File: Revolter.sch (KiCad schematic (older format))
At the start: 31 parts, among them J1 IO, J2 USB_A, P2 CAN, P3 IN+, P4 IN-, P5 MOTOR3, P6 MOTOR2, P7 MOTOR1, P9 Motor

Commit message: - removed lots of unused circuitry - implemented new DMOS power stage - power supplies still missing - removed rescue lib and fixed referenced
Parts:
- removed J1: IO, Connector_Phoenix_MC:PhoenixContact_MCV_1,5_8-G-3.5_1x08_P3.50mm_Vertical, symbol Revolter-rescue:Conn_01x08-conn
- removed JP1: Jumper_NC_Dual, Jumper:SolderJumper-3_P1.3mm_Open_RoundedPad1.0x1.5mm, symbol Device:Jumper_NC_Dual
- removed JP3, JP4: opt., Jumper:SolderJumper-2_P1.3mm_Open_RoundedPad1.0x1.5mm, symbol Device:Jumper_NC_Small
- removed P2: CAN, Connector_Phoenix_MC:PhoenixContact_MCV_1,5_4-G-3.5_1x04_P3.50mm_Vertical, symbol Revolter-rescue:CONN_01X04
- removed P9: Motor, Connector_Phoenix_MC:PhoenixContact_MCV_1,5_6-G-3.5_1x06_P3.50mm_Vertical, symbol Revolter-rescue:CONN_01X06
- removed R11, R61: 1k, Resistor_SMD:R_0805_2012Metric, symbol Device:R
- removed R62, R63: 1k5, Resistor_SMD:R_0805_2012Metric, symbol Device:R
- D13: symbol Revolter-rescue:ZENER-RESCUE-Revolter -> Device:D_Zener
- D2: value LED -> BLUE; symbol Revolter-rescue:LED-RESCUE-BLDC_4 -> Device:LED
- D3, D4: symbol Revolter-rescue:LED-RESCUE-BLDC_4 -> Device:LED
- J2: symbol Revolter-rescue:USB_A-conn -> Connector:USB_A
- P3, P4, P5, P6, P7: symbol Revolter-rescue:CONN_1 -> Connector_Generic:Conn_01x01
- R10, R4, R5, R6: symbol Revolter-rescue:R-RESCUE-BLDC_4 -> Device:R
- R9: symbol Revolter-rescue:R-RESCUE-BLDC_4 -> Device:Thermistor_NTC
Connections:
- net labels removed: +12V, +5V
- wire segments 90 -> 30
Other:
- note added: "REVOLTER 40V"
- note removed: "REVOLTER 100V"
- moved on the sheet: R8

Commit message: - added temp sensors and fan/pump outputs - made footprint selection
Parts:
- removed J2: USB_A, Connector_USB:USB_B_TE_5787834_Vertical, symbol Connector:USB_A
- added J1: Motor, symbol Connector_Generic:Conn_01x06
- added J2: TEMP, symbol Connector_Generic:Conn_01x12
- added J3: USB_B_Mini, Connector_USB:USB_Mini-B_Tensility_54-00023_Vertical, symbol Connector:USB_B_Mini
- added Q1, Q2, Q3: Q_NMOS_GSD, Package_TO_SOT_SMD:SOT-23, symbol Device:Q_NMOS_GSD
- added RN1, RN2, RN3: 10k, Resistor_SMD:R_Array_Convex_4x0603, symbol Device:R_Pack04
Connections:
- net labels added: +12V, FAN1, FAN2, PUMP, TEMP1, TEMP2, TEMP3
- wire segments 30 -> 79
- no-connect marks 0 -> 6
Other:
- moved on the sheet: P5, P6, P7

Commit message: - did most of the layout
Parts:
- removed D13: 3V3, Diode_SMD:D_SOD-123, symbol Device:D_Zener
- J1: footprint (none) -> Connector_PinHeader_2.00mm:PinHeader_1x06_P2.00mm_Vertical
- J2: footprint (none) -> Connector_PinHeader_2.00mm:PinHeader_1x12_P2.00mm_Vertical
- R4: value 470R -> 120R
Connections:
- wire segments 79 -> 78
- no-connect marks 6 -> 4
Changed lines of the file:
@@
 P 4750 5350
 F 0 "R4" V 4650 5350 50  0000 C CNN
-F 1 "470R" V 4750 5350 50  0000 C CNN
+F 1 "120R" V 4750 5350 50  0000 C CNN
 F 2 "Resistor_SMD:R_0805_2012Metric" H 4750 5350 60  0001 C CNN
 F 3 "" H 4750 5350 60  0001 C CNN
@@
 Wire Wire Line
 	5950 3700 5950 6500
-$Comp
-L Device:D_Zener D13
-U 1 1 599A9D56
-P 5450 4650
-F 0 "D13" H 5450 4750 50  0000 C CNN
-F 1 "3V3" H 5450 4550 50  0000 C CNN
-F 2 "Diode_SMD:D_SOD-123" H 5450 4650 50  0001 C CNN
-F 3 "" H 5450 4650 50  0000 C CNN
-	1    5450 4650
-	0    1    1    0
-$EndComp
-$Comp
-L power:GND #PWR015
-U 1 1 599AD91E
-P 5450 4800
-F 0 "#PWR015" H 5450 4800 30  0001 C CNN
-F 1 "GND" H 5450 4730 30  0001 C CNN
-F 2 "" H 5450 4800 60  0001 C CNN
-F 3 "" H 5450 4800 60  0001 C CNN
-	1    5450 4800
-	1    0    0    -1
-$EndComp
-Wire Wire Line
-	5200 4500 5450 4500
 Wire Wire Line
 	4300 3600 6150 3600
@@
 	2650 7050 2650 6600
 Wire Wire Line
-	2550 5100 2550 6250
-Wire Wire Line
-	2550 5100 2950 5100
+	2450 5100 2450 6250
+Wire Wire Line
+	2450 5100 2950 5100
 $Comp
 L power:GND #PWR0182
@@
 F 0 "J2" H 650 4600 50  0000 C CNN
 F 1 "TEMP" V 750 5300 50  0000 C CNN
-F 2 "" H 650 5300 50  0001 C CNN
+F 2 "Connector_PinHeader_2.00mm:PinHeader_1x12_P2.00mm_Vertical" H 650 5300 50  0001 C CNN
 F 3 "~" H 650 5300 50  0001 C CNN
 	1    650  5300
@@
 Connection ~ 2650 4900
 Wire Wire Line
-	1500 6250 2550 6250
+	1500 6250 2450 6250
 Wire Wire Line
 	1900 6600 2650 6600
@@
 Wire Wire Line
 	2000 7350 2000 7150
-$Comp
-L power:+3V3 #PWR0191
-U 1 1 5EF7F583
-P 2450 3650
-F 0 "#PWR0191" H 2450 3500 50  0001 C CNN
-F 1 "+3V3" H 2450 3850 50  0000 C CNN
-F 2 "" H 2450 3650 60  0000 C CNN
-F 3 "" H 2450 3650 60  0000 C CNN
-	1    2450 3650
-	-1   0    0    -1
-$EndComp
-Wire Wire Line
-	2450 4200 2450 4050
-Wire Wire Line
-	2150 4300 2150 4050
+Wire Wire Line
+	2050 4300 2050 4050
 $Comp
 L power:GND #PWR0192
@@
 F 0 "J1" H 650 4600 50  0000 C CNN
 F 1 "Motor" V 750 4300 50  0000 C CNN
-F 2 "" H 650 4300 50  0001 C CNN
+F 2 "Connector_PinHeader_2.00mm:PinHeader_1x06_P2.00mm_Vertical" H 650 4300 50  0001 C CNN
 F 3 "~" H 650 4300 50  0001 C CNN
 	1    650  4300
@@
 $EndComp
 Wire Wire Line
-	2950 4200 2450 4200
-Connection ~ 2450 4200
-Wire Wire Line
-	2450 4200 850  4200
-Wire Wire Line
-	850  4300 2150 4300
-Connection ~ 2150 4300
-Wire Wire Line
-	2150 4300 2950 4300
+	850  4300 2050 4300
+Connection ~ 2050 4300
+Wire Wire Line
+	2050 4300 2950 4300
 $Comp
 L Device:R_Pack04 RN2
@@
 	1    0    0    -1
 $EndComp
-Wire Wire Line
-	1600 5000 2550 5000
-Wire Wire Line
-	2550 4050 2550 5000
-Connection ~ 2550 5000
-Wire Wire Line
-	2550 5000 2950 5000
 $Comp
 L power:+3V3 #PWR0194
@@
 $EndComp
 Wire Wire Line
-	850  4400 2050 4400
-Wire Wire Line
-	850  4500 1950 4500
-Wire Wire Line
-	2050 4050 2050 4400
-Connection ~ 2050 4400
-Wire Wire Line
-	2050 4400 2950 4400
-Wire Wire Line
-	1950 4050 1950 4500
-Connection ~ 1950 4500
-Wire Wire Line
-	1950 4500 2950 4500
+	850  4400 1950 4400
+Wire Wire Line
+	850  4500 1850 4500
+Wire Wire Line
+	1950 4050 1950 4400
+Connection ~ 1950 4400
+Wire Wire Line
+	1950 4400 2950 4400
+Wire Wire Line
+	1850 4050 1850 4500
+Connection ~ 1850 4500
+Wire Wire Line
+	1850 4500 2950 4500
 $Comp
 L Device:R_Pack04 RN3
@@
 	1    0    0    -1
 $EndComp
-Wire Wire Line
-	2550 6250 2550 7050
-Connection ~ 2550 6250
 $Comp
 L power:GND #PWR0197
@@
 	1    0    0    -1
 $EndComp
-NoConn ~ 1850 3650
-NoConn ~ 1850 4050
-NoConn ~ 2450 7050
-NoConn ~ 2450 7450
 $Comp
 L Connector_Generic:Conn_01x01 P7
@@
 Wire Wire Line
 	8150 2850 7650 2850
+$Comp
+L power:+3V3 #PWR0164
+U 1 1 5F0837B1
+P 1850 3650
+F 0 "#PWR0164" H 1850 3500 50  0001 C CNN
+F 1 "+3V3" H 1850 3850 50  0000 C CNN
+F 2 "" H 1850 3650 60  0000 C CNN
+F 3 "" H 1850 3650 60  0000 C CNN
+	1    1850 3650
+	-1   0    0    -1
+$EndComp
+Wire Wire Line
+	2150 4050 2150 4200
+Connection ~ 2150 4200
+Wire Wire Line
+	2150 4200 850  4200
+Wire Wire Line
+	2150 4200 2950 4200
+Wire Wire Line
+	1600 5000 2450 5000
+NoConn ~ 2550 4050
+Wire Wire Line
+	2450 4050 2450 5000
+Connection ~ 2450 5000
+Wire Wire Line
+	2450 5000 2950 5000
+$Comp
+L power:+3V3 #PWR0165
+U 1 1 5F09E502
+P 2450 3650
+F 0 "#PWR0165" H 2450 3500 50  0001 C CNN
+F 1 "+3V3" H 2450 3850 50  0000 C CNN
+F 2 "" H 2450 3650 60  0000 C CNN
+F 3 "" H 2450 3650 60  0000 C CNN
+	1    2450 3650
+	-1   0    0    -1
+$EndComp
+Wire Wire Line
+	2450 7050 2450 6250
+Connection ~ 2450 6250
+$Comp
+L power:GND #PWR0175
+U 1 1 5F0ABB53
+P 2450 7450
+F 0 "#PWR0175" H 2450 7200 50  0001 C CNN
+F 1 "GND" H 2450 7200 50  0000 C CNN
+F 2 "" H 2450 7450 50  0001 C CNN
+F 3 "" H 2450 7450 50  0001 C CNN
+	1    2450 7450
+	1    0    0    -1
+$EndComp
+NoConn ~ 2550 7050
 $EndSCHEMATC

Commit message: - changed current sensors - updated symbols - exported for production
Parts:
- NT1: symbol Device:Net-Tie_2 -> Device:NetTie_2
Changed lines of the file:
@@
 	4300 3600 6150 3600
 $Comp
-L Device:Net-Tie_2 NT1
+L Device:NetTie_2 NT1
 U 1 1 5C9626AB
 P 8650 4800

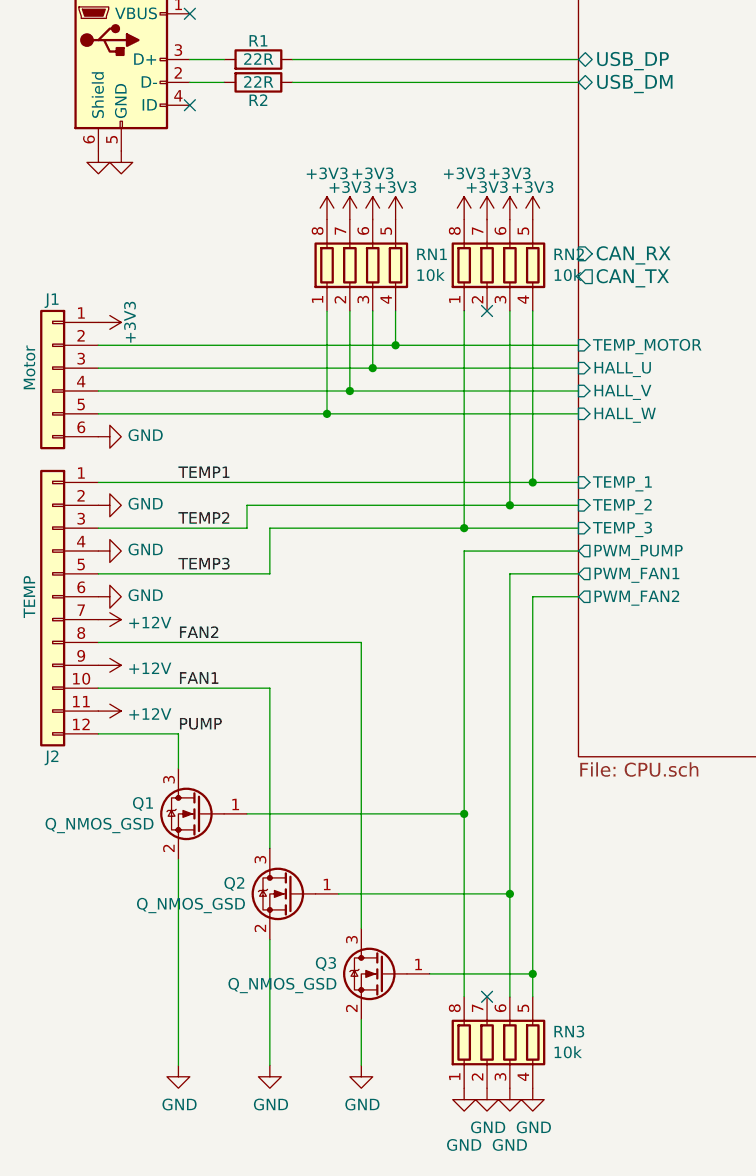
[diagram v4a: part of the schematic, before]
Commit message: - shrink PCB to 50x50mm
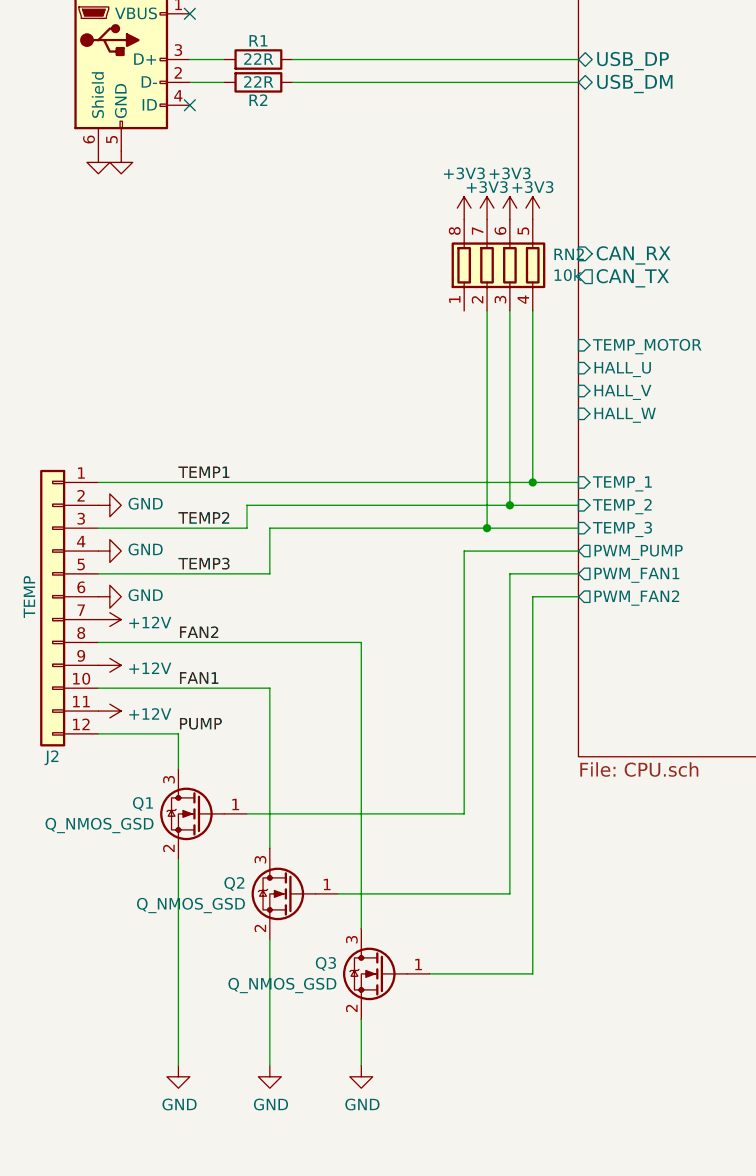
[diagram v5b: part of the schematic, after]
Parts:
- removed J1: Motor, Connector_PinHeader_2.00mm:PinHeader_1x06_P2.00mm_Vertical, symbol Connector_Generic:Conn_01x06
- removed RN1, RN3: 10k, Resistor_SMD:R_Array_Convex_4x0603, symbol Device:R_Pack04
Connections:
- net TEMP3: now also RN2.2 (R2.1); no longer RN2.1 (R1.1)
- no-connect marks 4 -> 2
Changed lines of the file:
@@
 	2950 5200 2650 5200
 Wire Wire Line
-	2750 7050 2750 6950
-Wire Wire Line
 	2750 5300 2950 5300
-Wire Wire Line
-	2650 7050 2650 6600
 Wire Wire Line
 	2450 5100 2450 6250
@@
 Wire Wire Line
 	1900 6600 2650 6600
-Connection ~ 2650 6600
 Wire Wire Line
 	2650 6600 2650 5200
 Wire Wire Line
 	2300 6950 2750 6950
-Connection ~ 2750 6950
 Wire Wire Line
 	2750 6950 2750 5300
 Wire Wire Line
 	2000 7350 2000 7150
-Wire Wire Line
-	2050 4300 2050 4050
-$Comp
-L power:GND #PWR0192
-U 1 1 5EF8ED65
-P 850 4600
-F 0 "#PWR0192" H 850 4350 50  0001 C CNN
-F 1 "GND" V 855 4472 50  0000 R CNN
-F 2 "" H 850 4600 50  0001 C CNN
-F 3 "" H 850 4600 50  0001 C CNN
-	1    850  4600
-	0    -1   -1   0
-$EndComp
-$Comp
-L power:+3V3 #PWR0193
-U 1 1 5EF8F1FA
-P 850 4100
-F 0 "#PWR0193" H 850 3950 50  0001 C CNN
-F 1 "+3V3" H 850 4240 50  0000 C CNN
-F 2 "" H 850 4100 60  0000 C CNN
-F 3 "" H 850 4100 60  0000 C CNN
-	1    850  4100
-	0    1    -1   0
-$EndComp
-$Comp
-L Connector_Generic:Conn_01x06 J1
-U 1 1 5EF904A4
-P 650 4300
-F 0 "J1" H 650 4600 50  0000 C CNN
-F 1 "Motor" V 750 4300 50  0000 C CNN
-F 2 "Connector_PinHeader_2.00mm:PinHeader_1x06_P2.00mm_Vertical" H 650 4300 50  0001 C CNN
-F 3 "~" H 650 4300 50  0001 C CNN
-	1    650  4300
-	-1   0    0    -1
-$EndComp
-Wire Wire Line
-	850  4300 2050 4300
-Connection ~ 2050 4300
-Wire Wire Line
-	2050 4300 2950 4300
 $Comp
 L Device:R_Pack04 RN2
@@
 $EndComp
 $Comp
-L power:+3V3 #PWR0194
-U 1 1 5EFB97D2
-P 2150 3650
-F 0 "#PWR0194" H 2150 3500 50  0001 C CNN
-F 1 "+3V3" H 2150 3790 50  0000 C CNN
-F 2 "" H 2150 3650 60  0000 C CNN
-F 3 "" H 2150 3650 60  0000 C CNN
-	1    2150 3650
-	-1   0    0    -1
-$EndComp
-$Comp
-L power:+3V3 #PWR0195
-U 1 1 5EFB97DC
-P 2050 3650
-F 0 "#PWR0195" H 2050 3500 50  0001 C CNN
-F 1 "+3V3" H 2050 3850 50  0000 C CNN
-F 2 "" H 2050 3650 60  0000 C CNN
-F 3 "" H 2050 3650 60  0000 C CNN
-	1    2050 3650
-	-1   0    0    -1
-$EndComp
-$Comp
-L power:+3V3 #PWR0196
-U 1 1 5EFB97E6
-P 1950 3650
-F 0 "#PWR0196" H 1950 3500 50  0001 C CNN
-F 1 "+3V3" H 1950 3790 50  0000 C CNN
-F 2 "" H 1950 3650 60  0000 C CNN
-F 3 "" H 1950 3650 60  0000 C CNN
-	1    1950 3650
-	-1   0    0    -1
-$EndComp
-$Comp
-L Device:R_Pack04 RN1
-U 1 1 5EFB97FA
-P 2050 3850
-F 0 "RN1" H 2238 3896 50  0000 L CNN
-F 1 "10k" H 2238 3805 50  0000 L CNN
-F 2 "Resistor_SMD:R_Array_Convex_4x0603" V 2325 3850 50  0001 C CNN
-F 3 "~" H 2050 3850 50  0001 C CNN
-	1    2050 3850
-	1    0    0    -1
-$EndComp
-Wire Wire Line
-	850  4400 1950 4400
-Wire Wire Line
-	850  4500 1850 4500
-Wire Wire Line
-	1950 4050 1950 4400
-Connection ~ 1950 4400
-Wire Wire Line
-	1950 4400 2950 4400
-Wire Wire Line
-	1850 4050 1850 4500
-Connection ~ 1850 4500
-Wire Wire Line
-	1850 4500 2950 4500
-$Comp
-L Device:R_Pack04 RN3
-U 1 1 5EFC6BA8
-P 2650 7250
-F 0 "RN3" H 2838 7296 50  0000 L CNN
-F 1 "10k" H 2838 7205 50  0000 L CNN
-F 2 "Resistor_SMD:R_Array_Convex_4x0603" V 2925 7250 50  0001 C CNN
-F 3 "~" H 2650 7250 50  0001 C CNN
-	1    2650 7250
-	1    0    0    -1
-$EndComp
-$Comp
-L power:GND #PWR0197
-U 1 1 5EFD0BBD
-P 2550 7450
-F 0 "#PWR0197" H 2550 7200 50  0001 C CNN
-F 1 "GND" H 2555 7277 50  0000 C CNN
-F 2 "" H 2550 7450 50  0001 C CNN
-F 3 "" H 2550 7450 50  0001 C CNN
-	1    2550 7450
-	1    0    0    -1
-$EndComp
-$Comp
-L power:GND #PWR0198
-U 1 1 5EFD121F
-P 2650 7450
-F 0 "#PWR0198" H 2650 7200 50  0001 C CNN
-F 1 "GND" H 2650 7200 50  0000 C CNN
-F 2 "" H 2650 7450 50  0001 C CNN
-F 3 "" H 2650 7450 50  0001 C CNN
-	1    2650 7450
-	1    0    0    -1
-$EndComp
-$Comp
-L power:GND #PWR0199
-U 1 1 5EFD1402
-P 2750 7450
-F 0 "#PWR0199" H 2750 7200 50  0001 C CNN
-F 1 "GND" H 2755 7277 50  0000 C CNN
-F 2 "" H 2750 7450 50  0001 C CNN
-F 3 "" H 2750 7450 50  0001 C CNN
-	1    2750 7450
-	1    0    0    -1
-$EndComp
-$Comp
 L Connector_Generic:Conn_01x01 P7
 U 1 1 5895E680
@@
 	8150 2850 7650 2850
 $Comp
-L power:+3V3 #PWR0164
-U 1 1 5F0837B1
-P 1850 3650
-F 0 "#PWR0164" H 1850 3500 50  0001 C CNN
-F 1 "+3V3" H 1850 3850 50  0000 C CNN
-F 2 "" H 1850 3650 60  0000 C CNN
-F 3 "" H 1850 3650 60  0000 C CNN
-	1    1850 3650
-	-1   0    0    -1
-$EndComp
-Wire Wire Line
-	2150 4050 2150 4200
-Connection ~ 2150 4200
-Wire Wire Line
-	2150 4200 850  4200
-Wire Wire Line
-	2150 4200 2950 4200
-Wire Wire Line
-	1600 5000 2450 5000
-NoConn ~ 2550 4050
-Wire Wire Line
-	2450 4050 2450 5000
-Connection ~ 2450 5000
-Wire Wire Line
-	2450 5000 2950 5000
-$Comp
 L power:+3V3 #PWR0165
 U 1 1 5F09E502
@@
 $EndComp
 Wire Wire Line
-	2450 7050 2450 6250
-Connection ~ 2450 6250
-$Comp
-L power:GND #PWR0175
-U 1 1 5F0ABB53
-P 2450 7450
-F 0 "#PWR0175" H 2450 7200 50  0001 C CNN
-F 1 "GND" H 2450 7200 50  0000 C CNN
-F 2 "" H 2450 7450 50  0001 C CNN
-F 3 "" H 2450 7450 50  0001 C CNN
-	1    2450 7450
-	1    0    0    -1
-$EndComp
-NoConn ~ 2550 7050
+	1600 5000 2550 5000
+Wire Wire Line
+	2550 4050 2550 5000
+Connection ~ 2550 5000
+Wire Wire Line
+	2550 5000 2950 5000
 $EndSCHEMATC

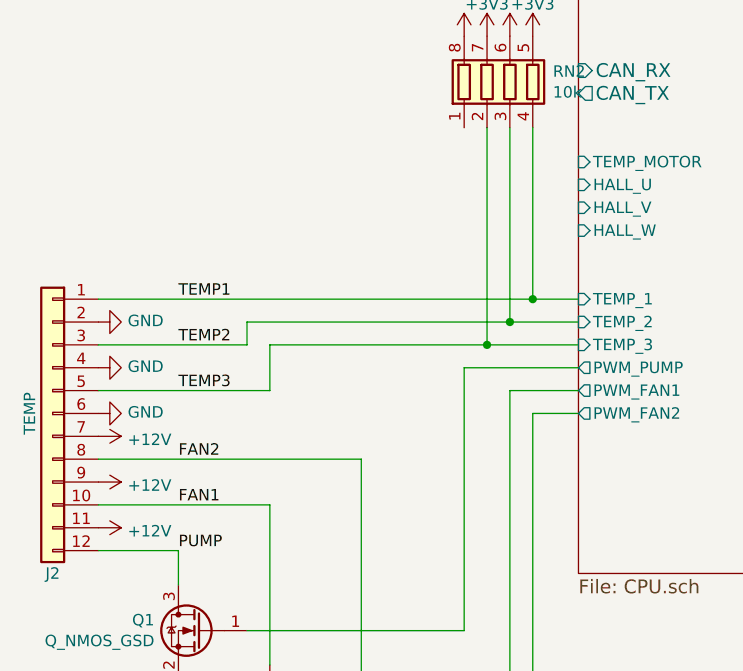
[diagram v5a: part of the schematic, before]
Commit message: - added flyback diodes to FAN outputs - added fourth DC cap - changed TEMP3 to motor temp
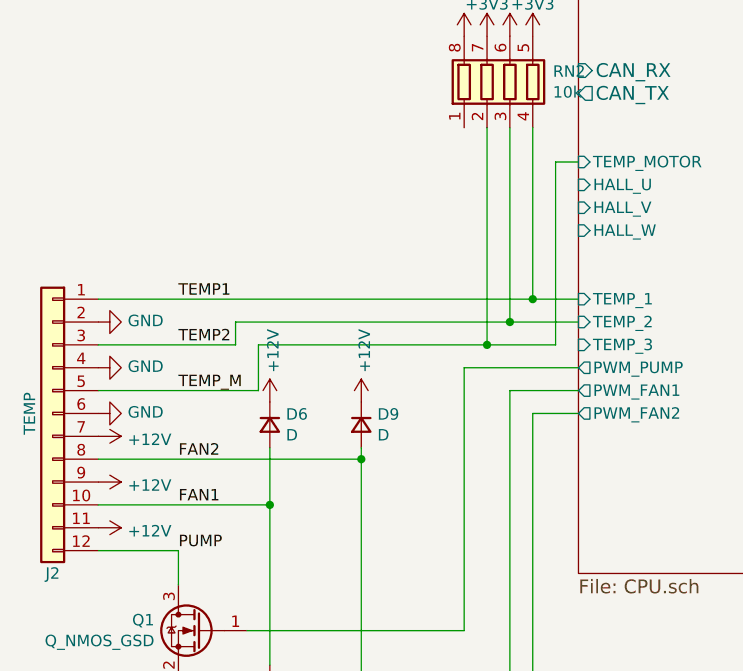
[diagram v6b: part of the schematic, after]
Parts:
- added D6, D9: D, Diode_SMD:D_SOD-123, symbol Device:D_Small
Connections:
- net +12V: now also D6.1 (K), D9.1 (K)
- net FAN1: now also D6.2 (A)
- net FAN2: now also D9.2 (A)
- net TEMP3 renamed TEMP_M
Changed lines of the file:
@@
 	2750 4050 2750 4800
-Wire Wire Line
-	2750 4800 2950 4800
 Wire Wire Line
 	2950 4900 2650 4900
@@
 	2000 5500 2000 6750
 Wire Wire Line
-	1600 5200 1600 5000
-Wire Wire Line
-	850  5200 1600 5200
-Wire Wire Line
-	850  5000 1500 5000
-Connection ~ 2750 4800
+	1550 5200 1550 5000
+Wire Wire Line
+	850  5200 1550 5200
+Wire Wire Line
+	850  5000 1450 5000
 Wire Wire Line
 	850  5900 1200 5900
@@
 	0    1    1    0
 $EndComp
-Text Label 1200 4800 0    50   ~ 0
-TEMP1
 Text Label 1200 5000 0    50   ~ 0
 TEMP2
 Text Label 1200 5200 0    50   ~ 0
-TEMP3
+TEMP_M
 Text Label 1200 5900 0    50   ~ 0
 PUMP
@@
 	850  4800 2750 4800
 Wire Wire Line
-	1500 5000 1500 4900
-Wire Wire Line
-	1500 4900 2650 4900
+	1450 5000 1450 4900
+Wire Wire Line
+	1450 4900 2650 4900
 Connection ~ 2650 4900
 Wire Wire Line
@@
 $EndComp
 Wire Wire Line
-	1600 5000 2550 5000
+	1550 5000 2550 5000
 Wire Wire Line
 	2550 4050 2550 5000
+$Comp
+L Device:D_Small D9
+U 1 1 5FCC59B8
+P 2000 5350
+F 0 "D9" V 1954 5420 50  0000 L CNN
+F 1 "D" V 2045 5420 50  0000 L CNN
+F 2 "Diode_SMD:D_SOD-123" V 2000 5350 50  0001 C CNN
+F 3 "~" V 2000 5350 50  0001 C CNN
+	1    2000 5350
+	0    1    1    0
+$EndComp
+Connection ~ 2000 5500
+$Comp
+L Device:D_Small D6
+U 1 1 5FCC6889
+P 1600 5350
+F 0 "D6" V 1554 5420 50  0000 L CNN
+F 1 "D" V 1645 5420 50  0000 L CNN
+F 2 "Diode_SMD:D_SOD-123" V 1600 5350 50  0001 C CNN
+F 3 "~" V 1600 5350 50  0001 C CNN
+	1    1600 5350
+	0    1    1    0
+$EndComp
+Wire Wire Line
+	2000 5450 2000 5500
+$Comp
+L power:+12V #PWR0175
+U 1 1 5FCCBD88
+P 1600 5250
+F 0 "#PWR0175" H 1600 5100 50  0001 C CNN
+F 1 "+12V" V 1615 5378 50  0000 L CNN
+F 2 "" H 1600 5250 50  0001 C CNN
+F 3 "" H 1600 5250 50  0001 C CNN
+	1    1600 5250
+	1    0    0    -1
+$EndComp
+$Comp
+L power:+12V #PWR0192
+U 1 1 5FCCCC45
+P 2000 5250
+F 0 "#PWR0192" H 2000 5100 50  0001 C CNN
+F 1 "+12V" V 2015 5378 50  0000 L CNN
+F 2 "" H 2000 5250 50  0001 C CNN
+F 3 "" H 2000 5250 50  0001 C CNN
+	1    2000 5250
+	1    0    0    -1
+$EndComp
+Wire Wire Line
+	1600 5450 1600 5700
+Connection ~ 1600 5700
+Connection ~ 2750 4800
+Wire Wire Line
+	2750 4800 2950 4800
+Text Label 1200 4800 0    50   ~ 0
+TEMP1
+Wire Wire Line
+	2550 5000 2850 5000
+Wire Wire Line
+	2850 5000 2850 4200
+Wire Wire Line
+	2850 4200 2950 4200
 Connection ~ 2550 5000
-Wire Wire Line
-	2550 5000 2950 5000
 $EndSCHEMATC
